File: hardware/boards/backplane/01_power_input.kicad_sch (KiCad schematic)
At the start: 13 parts, among them J1 XT30U_2+2, J2 XT30U_2+2, J3 XT30U_2+2, J4 XT30U_2+2, J5 XT30U_2+2, J6 XT30U_2+2, J7 XY308-2.54-3P / EXTERNAL CAN, U5 TCAN3413DR

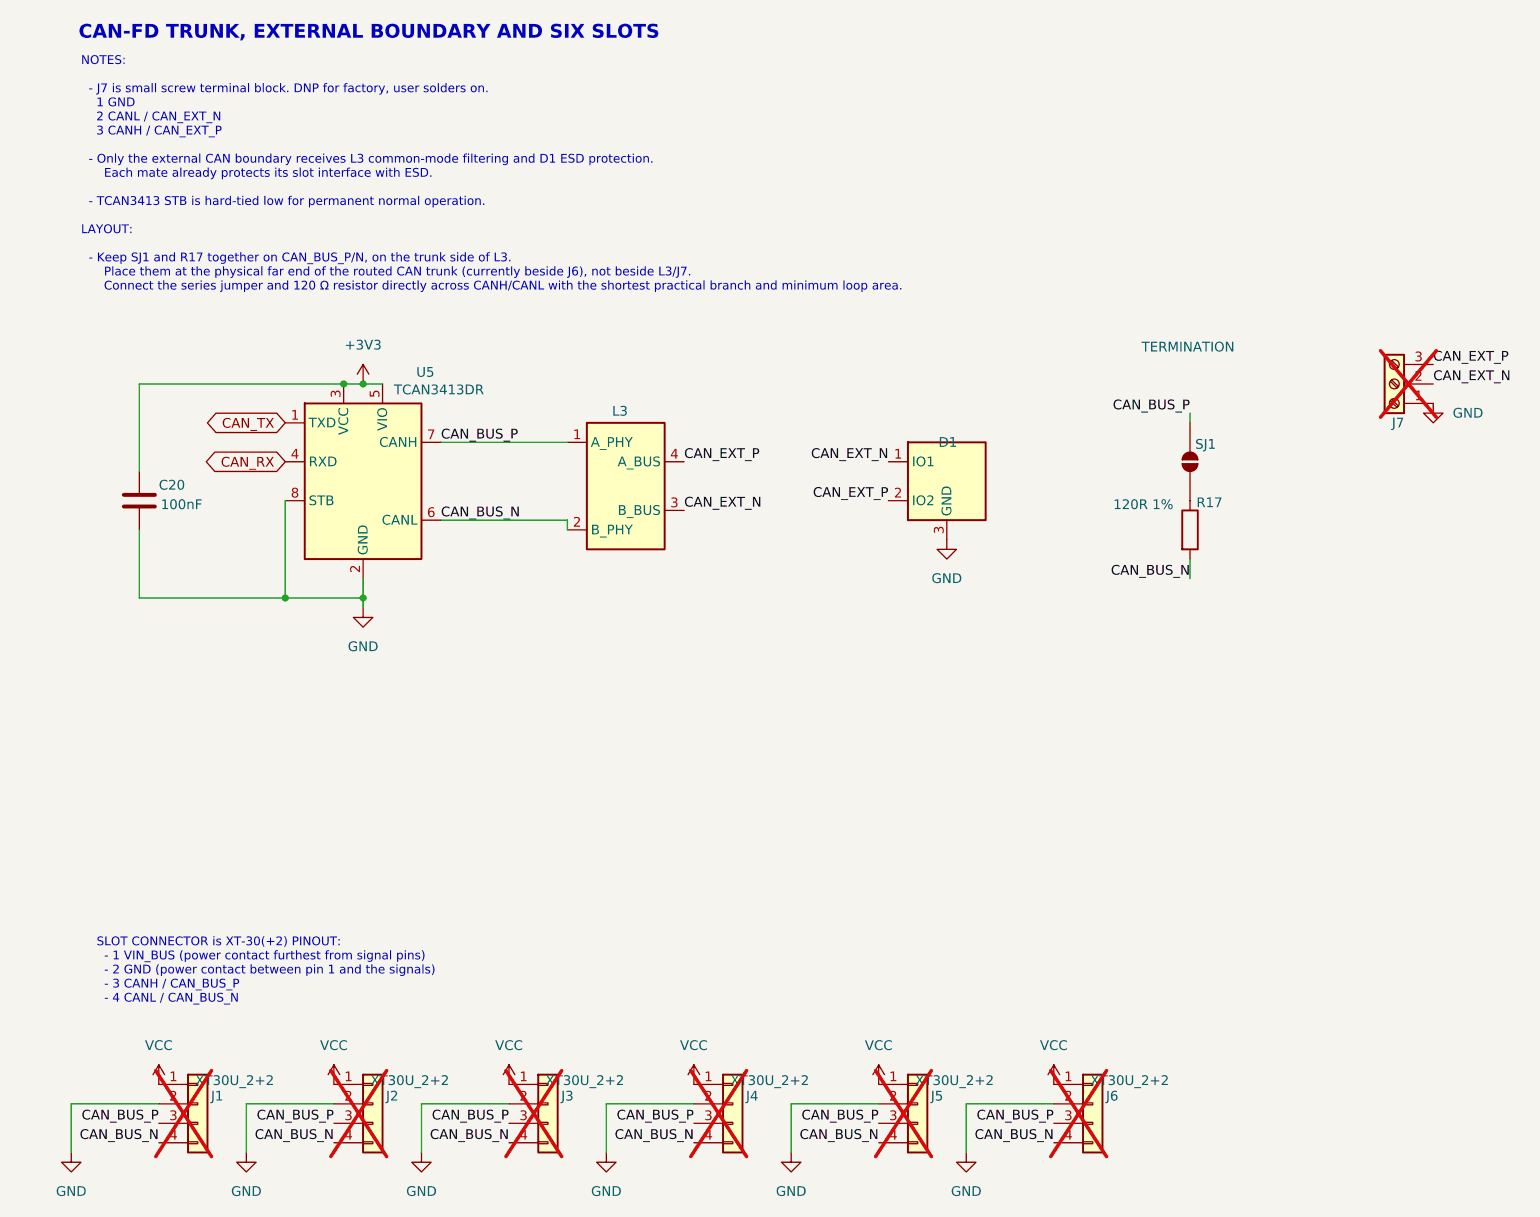
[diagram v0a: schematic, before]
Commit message: refactor: consolidate active KiCad projects under backplane and carrier
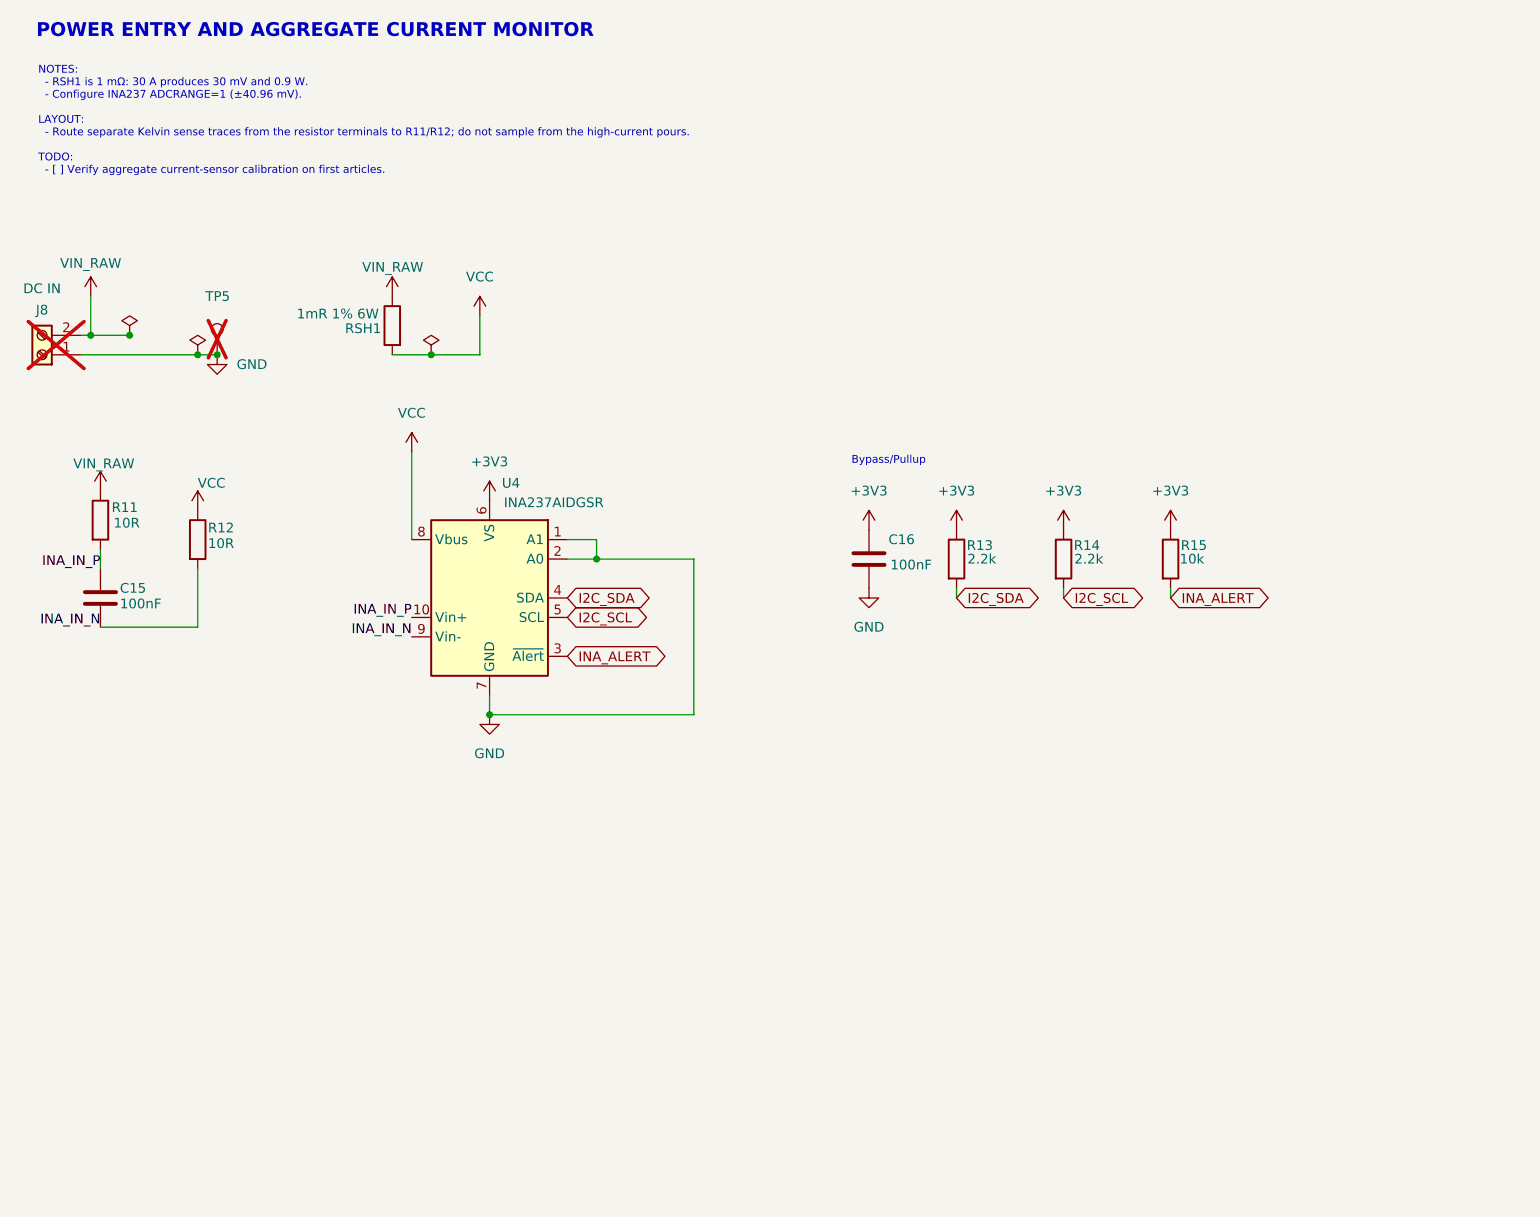
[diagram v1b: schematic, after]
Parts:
- removed C20: 100nF, Capacitor_SMD:C_0603_1608Metric, symbol Device:C
- removed D1: PESD2CANFD27V-TR, Package_TO_SOT_SMD:SOT-23, symbol backplane-backpack:PESD_Dual_SOT23
- removed J1, J2, J3, J4, J5, J6: XT30U_2+2, mini-rack-power:Amass_XT30U_2plus2_F, symbol Connector_Generic:Conn_01x04
- removed J7: XY308-2.54-3P / EXTERNAL CAN, mini-rack-power:TerminalBlock_Xinya_XY308-2.54-3P_1x03_P2.54mm_Horizontal, symbol Connector:Screw_Terminal_01x03
- removed L3: ACT1210D-101-2P-TL00, mini-rack-power:L_CommonModeChoke_TDK_ACT1210D, symbol backplane-backpack:ACT1210D_1243
- removed R17: 120R 1%, Resistor_SMD:R_0603_1608Metric, symbol Device:R
- removed SJ1: TERMINATION, Jumper:SolderJumper-2_P1.3mm_Open_Pad1.0x1.5mm, symbol Jumper:SolderJumper_2_Open
- removed U5: TCAN3413DR, Package_SO:SOIC-8_3.9x4.9mm_P1.27mm, symbol backplane-backpack:TCAN3413DR
- added C15, C16: 100nF, Capacitor_SMD:C_0603_1608Metric, symbol Device:C
- added J8: DC IN, mini-rack-power:DORABO_DB910-6.35-2P-GN-S, symbol Connector:Screw_Terminal_01x02
- added R11, R12: 10R, Resistor_SMD:R_0603_1608Metric, symbol Device:R
- added R13, R14: 2.2k, Resistor_SMD:R_0603_1608Metric, symbol Device:R
- added R15: 10k, Resistor_SMD:R_0603_1608Metric, symbol Device:R
- added RSH1: 1mR 1% 6W, Resistor_SMD:R_2512_6332Metric, symbol Device:R
- added TP5: GND, TestPoint:TestPoint_Pad_D1.5mm, symbol Connector:TestPoint
- added U4: INA237AIDGSR, mini-rack-power:MSOP-10_3x3mm_P0.5mm_0.20mm_Clearance, symbol Sensor_Energy:INA237
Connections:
- net +3V3: now also C16.1, R13.1, R14.1, R15.1, U4.6 (VS)
- net GND: now also C16.2, J8.1 (Pin_1), TP5.1, U4.1 (A1), U4.2 (A0), U4.7 (GND)
- net VCC: now also R12.1, RSH1.2, U4.8 (Vbus)
- new net I2C_SCL: R14.2, U4.5 (SCL)
- new net I2C_SDA: R13.2, U4.4 (SDA)
- new net INA_ALERT: R15.2, U4.3 (~{Alert})
- new net INA_IN_N: C15.2, R12.2, U4.9 (Vin-)
- new net INA_IN_P: C15.1, R11.2, U4.10 (Vin+)
- new net VIN_RAW: J8.2 (Pin_2), R11.1, RSH1.1
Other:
- note added: "Bypass/Pullup"
- note added: "NOTES: - RSH1 is 1 mΩ: 30 A produces 30 mV and 0.9 W. - Configure INA237 ADCRANGE=1 (±40.96 mV). LAYOUT: - Route separate Kelvin sense traces from the resistor terminals to R11/R12; do not sample from the high-current pours. TODO:r - [ ] Verify aggregate current-sensor calibration on first articles."
- note added: "POWER ENTRY AND AGGREGATE CURRENT MONITOR"
- note removed: "CAN-FD TRUNK, EXTERNAL BOUNDARY AND SIX SLOTS"
- note removed: "NOTES: - J7 is small screw terminal block. DNP for factory, user solders on. 1 GND 2 CANL / CAN_EXT_N 3 CANH / CAN_EXT_P - Only the external CAN boundary receives L3 common-mode filtering and D1 ESD protection. Each mate already protects its slot interface with ESD. - TCAN3413 STB is hard-tied low for permanent normal operation. LAYOUT: - Keep SJ1 and R17 together on CAN_BUS_P/N, on the trunk sid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"
- note removed: "SLOT CONNECTOR is XT-30(+2) PINOUT: - 1 VIN_BUS (power contact furthest from signal pins) - 2 GND (power contact between pin 1 and the signals) - 3 CANH / CAN_BUS_P - 4 CANL / CAN_BUS_N"

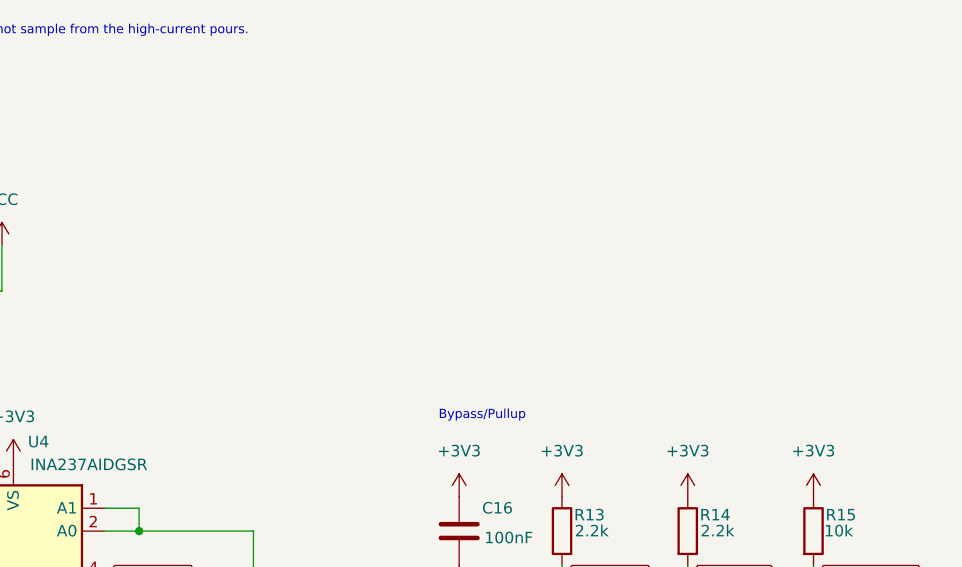
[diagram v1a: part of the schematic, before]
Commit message: docs(hardware): clarify carrier voltage limits and qualification TODOs
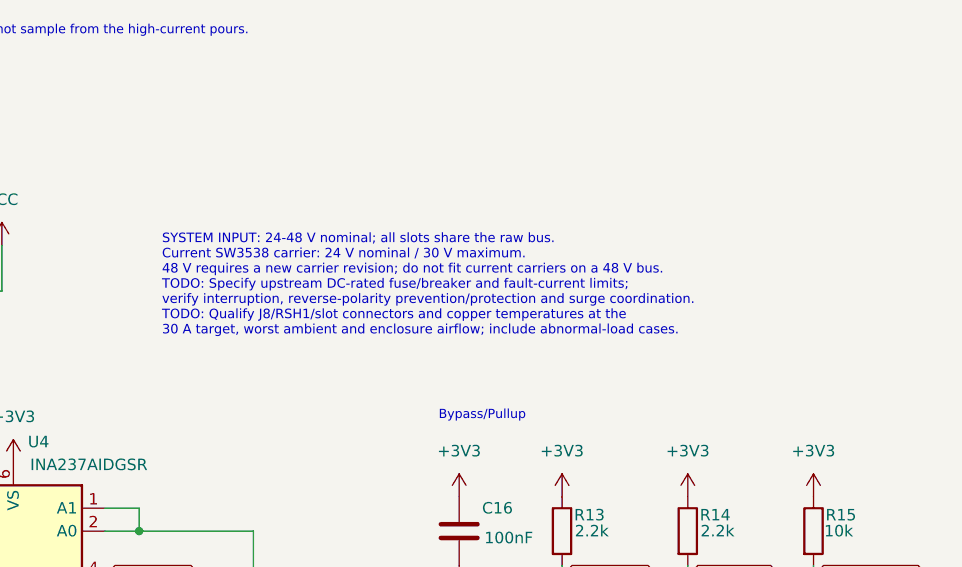
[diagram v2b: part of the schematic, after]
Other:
- note added: "NOTES: - RSH1 is 1 mΩ: 30 A produces 30 mV and 0.9 W. - Configure INA237 ADCRANGE=1 (±40.96 mV). LAYOUT: - Route separate Kelvin sense traces from the resistor terminals to R11/R12; do not sample from the high-current pours. TODO: - [ ] Verify aggregate current-sensor calibration on first articles."
- note added: "SYSTEM INPUT: 24-48 V nominal; all slots share the raw bus. Current SW3538 carrier: 24 V nominal / 30 V maximum. 48 V requires a new carrier revision; do not fit current carriers on a 48 V bus. TODO: Specify upstream DC-rated fuse/breaker and fault-current limits; verify interruption, reverse-polarity prevention/protection and surge coordination. TODO: Qualify J8/RSH1/slot connectors and copper t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"
- note removed: "NOTES: - RSH1 is 1 mΩ: 30 A produces 30 mV and 0.9 W. - Configure INA237 ADCRANGE=1 (±40.96 mV). LAYOUT: - Route separate Kelvin sense traces from the resistor terminals to R11/R12; do not sample from the high-current pours. TODO:r - [ ] Verify aggregate current-sensor calibration on first articles."
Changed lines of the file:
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@@
 	(generator_version "10.0")
 	(paper "A4")
-	(text "NOTES:\n  - RSH1 is 1 mΩ: 30 A produces 30 mV and 0.9 W.\n  - Configure INA237 ADCRANGE=1 (±40.96 mV).\n\nLAYOUT:\n  - Route separate Kelvin sense traces from the resistor terminals to R11/R12; do not sample from the high-current pours.\n\nTODO:\r\n  - [ ] Verify aggregate current-sensor calibration on first articles."
+	(text "SYSTEM INPUT: 24-48 V nominal; all slots share the raw bus.\nCurrent SW3538 carrier: 24 V nominal / 30 V maximum.\n48 V requires a new carrier revision; do not fit current carriers on a 48 V bus.\nTODO: Specify upstream DC-rated fuse/breaker and fault-current limits;\nverify interruption, reverse-polarity prevention/protection and surge coordination.\nTODO: Qualify J8/RSH1/slot connectors and copper temperatures at the\n30 A target, worst ambient and enclosure airflow; include abnormal-load cases."
+		(exclude_from_sim no)
+		(at 90.17 63.5 0)
+		(effects
+			(font
+				(size 1.05 1.05)
+			)
+			(justify left bottom)
+		)
+	)
+	(text "NOTES:\n  - RSH1 is 1 mΩ: 30 A produces 30 mV and 0.9 W.\n  - Configure INA237 ADCRANGE=1 (±40.96 mV).\n\nLAYOUT:\n  - Route separate Kelvin sense traces from the resistor terminals to R11/R12; do not sample from the high-current pours.\n\nTODO:\n  - [ ] Verify aggregate current-sensor calibration on first articles."
 		(exclude_from_sim no)
 		(at 14.732 35.052 0)

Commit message: Checkpoint backplane before CAN test point routing adjustments
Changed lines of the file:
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@@
 	(generator_version "10.0")
 	(paper "A4")
-	(text "SYSTEM INPUT: 24-48 V nominal; all slots share the raw bus.\nCurrent SW3538 carrier: 24 V nominal / 30 V maximum.\n48 V requires a new carrier revision; do not fit current carriers on a 48 V bus.\nTODO: Specify upstream DC-rated fuse/breaker and fault-current limits;\nverify interruption, reverse-polarity prevention/protection and surge coordination.\nTODO: Qualify J8/RSH1/slot connectors and copper temperatures at the\n30 A target, worst ambient and enclosure airflow; include abnormal-load cases."
-		(exclude_from_sim no)
-		(at 90.17 63.5 0)
-		(effects
-			(font
-				(size 1.05 1.05)
-			)
-			(justify left bottom)
-		)
-	)
 	(text "NOTES:\n  - RSH1 is 1 mΩ: 30 A produces 30 mV and 0.9 W.\n  - Configure INA237 ADCRANGE=1 (±40.96 mV).\n\nLAYOUT:\n  - Route separate Kelvin sense traces from the resistor terminals to R11/R12; do not sample from the high-current pours.\n\nTODO:\n  - [ ] Verify aggregate current-sensor calibration on first articles."
 		(exclude_from_sim no)
@@
 		)
 	)
+	(text "SYSTEM INPUT: 24-48 V nominal; all slots share the raw bus.\nCurrent SW3538 carrier: 24 V nominal / 30 V maximum.\n48 V requires a new carrier revision; do not fit current carriers on a 48 V bus.\nTODO: Specify upstream DC-rated fuse/breaker and fault-current limits;\nverify interruption, reverse-polarity prevention/protection and surge coordination.\nTODO: Qualify J8/RSH1/slot connectors and copper temperatures at the\n30 A target, worst ambient and enclosure airflow; include abnormal-load cases."
+		(exclude_from_sim no)
+		(at 90.17 63.5 0)
+		(effects
+			(font
+				(size 1.05 1.05)
+			)
+			(justify left bottom)
+		)
+	)
 	(text "POWER ENTRY AND AGGREGATE CURRENT MONITOR"
 		(exclude_from_sim no)
@@
 	)
 	(junction
-		(at 26.67 55.88)
-		(diameter 0)
-		(color 0 0 0 0)
-	)
-	(junction
